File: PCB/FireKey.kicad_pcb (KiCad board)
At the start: 2 copper layers, 99.7 x 99.1 mm, 71 parts, among them P1 Pad, P2 Pad, SW1 SW_MEC_4A, U1 Arduino_Pro_Micro_USB-C

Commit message: finished rounting
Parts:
- moved P1 25.6 mm to (163.6, 48.8)
- moved P2 23.5 mm to (169.7, 48.8)
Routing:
- net VCC: track 516.5 -> 527.2 mm
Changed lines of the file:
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@@
   )
   (footprint "TestPoint:TestPoint_Pad_D2.5mm" (layer "B.Cu")
-    (at 169.418 25.273 180)
+    (at 169.672 48.768 180)
     (descr "SMD pad as test Point, diameter 2.5mm")
     (tags "test point SMD pad")
@@
   )
   (footprint "TestPoint:TestPoint_Pad_D2.5mm" (layer "B.Cu")
-    (at 173.99 25.4 180)
+    (at 163.576 48.768 180)
     (descr "SMD pad as test Point, diameter 2.5mm")
     (tags "test point SMD pad")
@@
     (effects (font (size 0.75 0.75) (thickness 0.16)) (justify mirror))
   )
-  (gr_text "VCC" (at 165.481 27.94) (layer "B.SilkS")
+  (gr_text "VCC" (at 163.576 51.308) (layer "B.SilkS")
     (effects (font (size 1 1) (thickness 0.2)) (justify mirror))
   )
@@
     (effects (font (size 0.75 0.75) (thickness 0.16)) (justify mirror))
   )
-  (gr_text "GND" (at 169.418 27.94) (layer "B.SilkS")
+  (gr_text "GND" (at 169.672 51.308) (layer "B.SilkS")
     (effects (font (size 1 1) (thickness 0.2)) (justify mirror))
   )
@@
   (segment (start 157.607 89.408) (end 156.8185 90.1965) (width 0.635) (layer "B.Cu") (net 1))
   (segment (start 179.445 129.425) (end 175.8805 129.425) (width 0.635) (layer "B.Cu") (net 1))
+  (segment (start 164.865 40.875) (end 163.576 42.164) (width 0.635) (layer "B.Cu") (net 1))
   (segment (start 203.995 40.875) (end 203.995 39.845) (width 0.635) (layer "B.Cu") (net 1))
   (segment (start 233.0305 91.325) (end 233.0185 91.313) (width 0.635) (layer "B.Cu") (net 1))
@@
   (segment (start 213.9685 90.1965) (end 214.757 89.408) (width 0.635) (layer "B.Cu") (net 1))
   (segment (start 176.657 127.508) (end 157.607 127.508) (width 0.635) (layer "B.Cu") (net 1))
+  (segment (start 163.576 42.164) (end 163.576 48.768) (width 0.635) (layer "B.Cu") (net 1))
   (segment (start 233.0185 129.413) (end 233.0185 128.2965) (width 0.635) (layer "B.Cu") (net 1))
   (segment (start 223.145 111.875) (end 226.7095 111.875) (width 0.635) (layer "B.Cu") (net 1))
@@
   (segment (start 217.545 91.325) (end 213.9805 91.325) (width 0.635) (layer "B.Cu") (net 1))
   (segment (start 175.8685 129.413) (end 175.8685 128.2965) (width 0.635) (layer "B.Cu") (net 1))
+  (segment (start 167.165 40.875) (end 164.865 40.875) (width 0.635) (layer "B.Cu") (net 1))
   (segment (start 203.995 39.845) (end 204.724 39.116) (width 0.635) (layer "B.Cu") (net 1))
   (segment (start 175.8805 91.325) (end 175.8685 91.313) (width 0.635) (layer "B.Cu") (net 1))

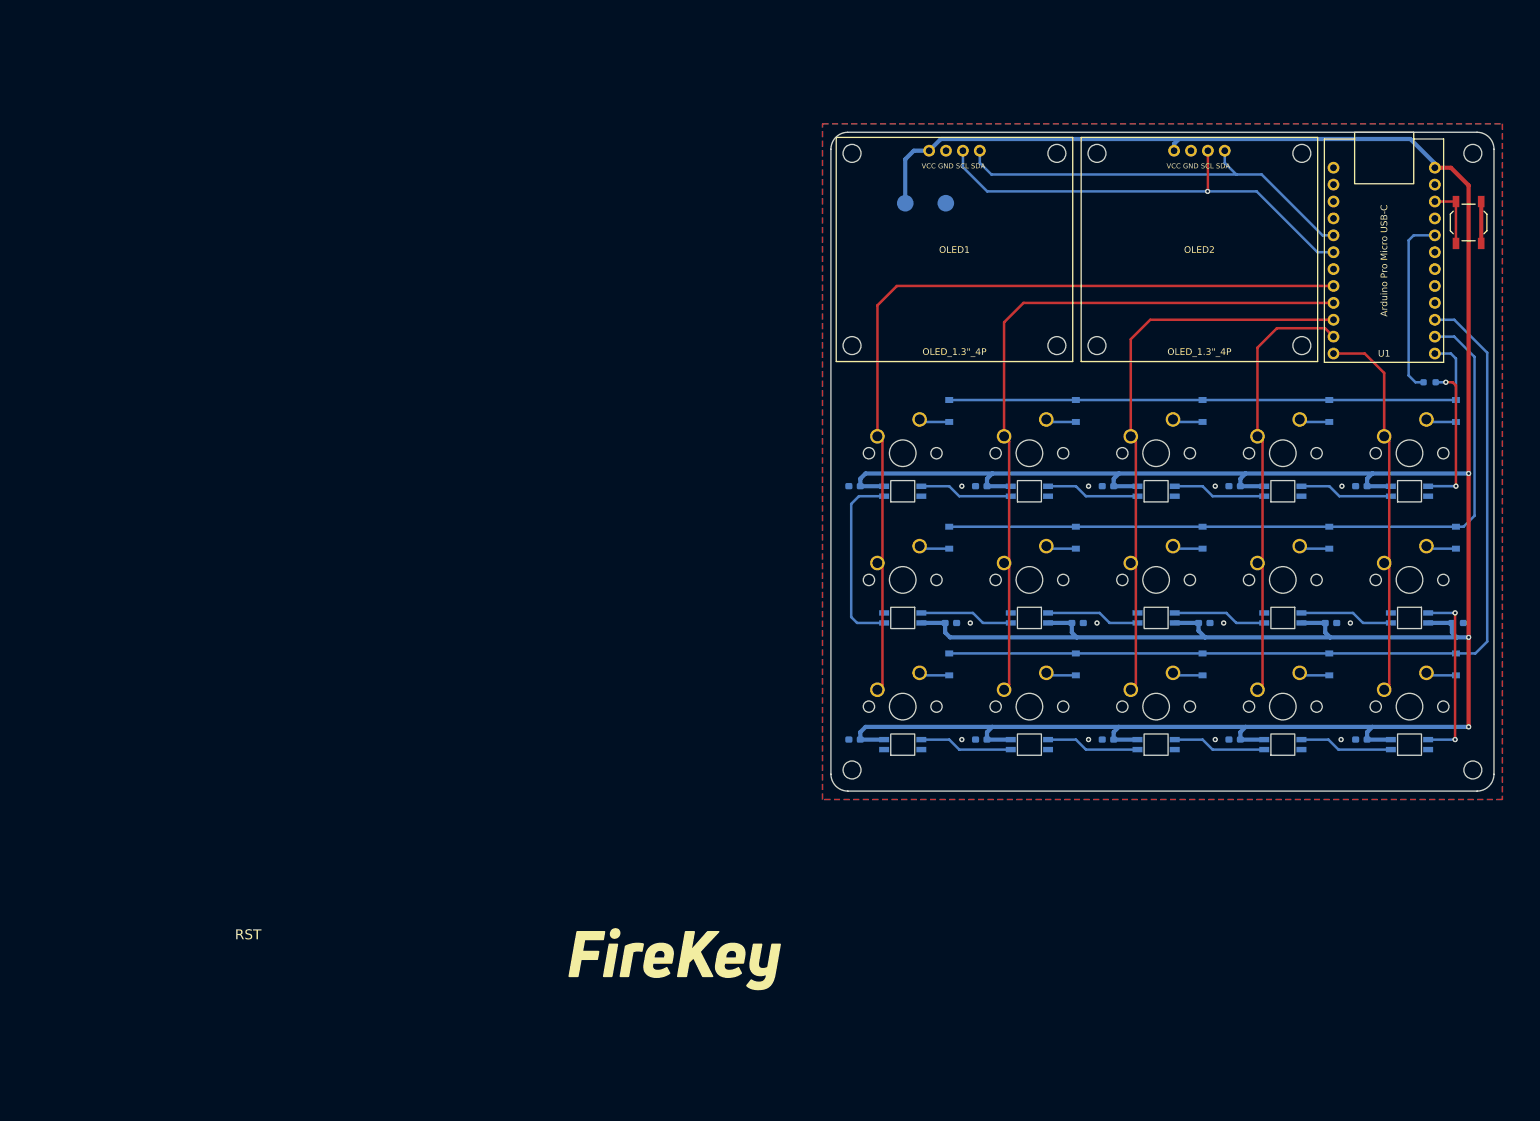
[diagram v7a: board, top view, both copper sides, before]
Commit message: small changes to PCB; placing logos
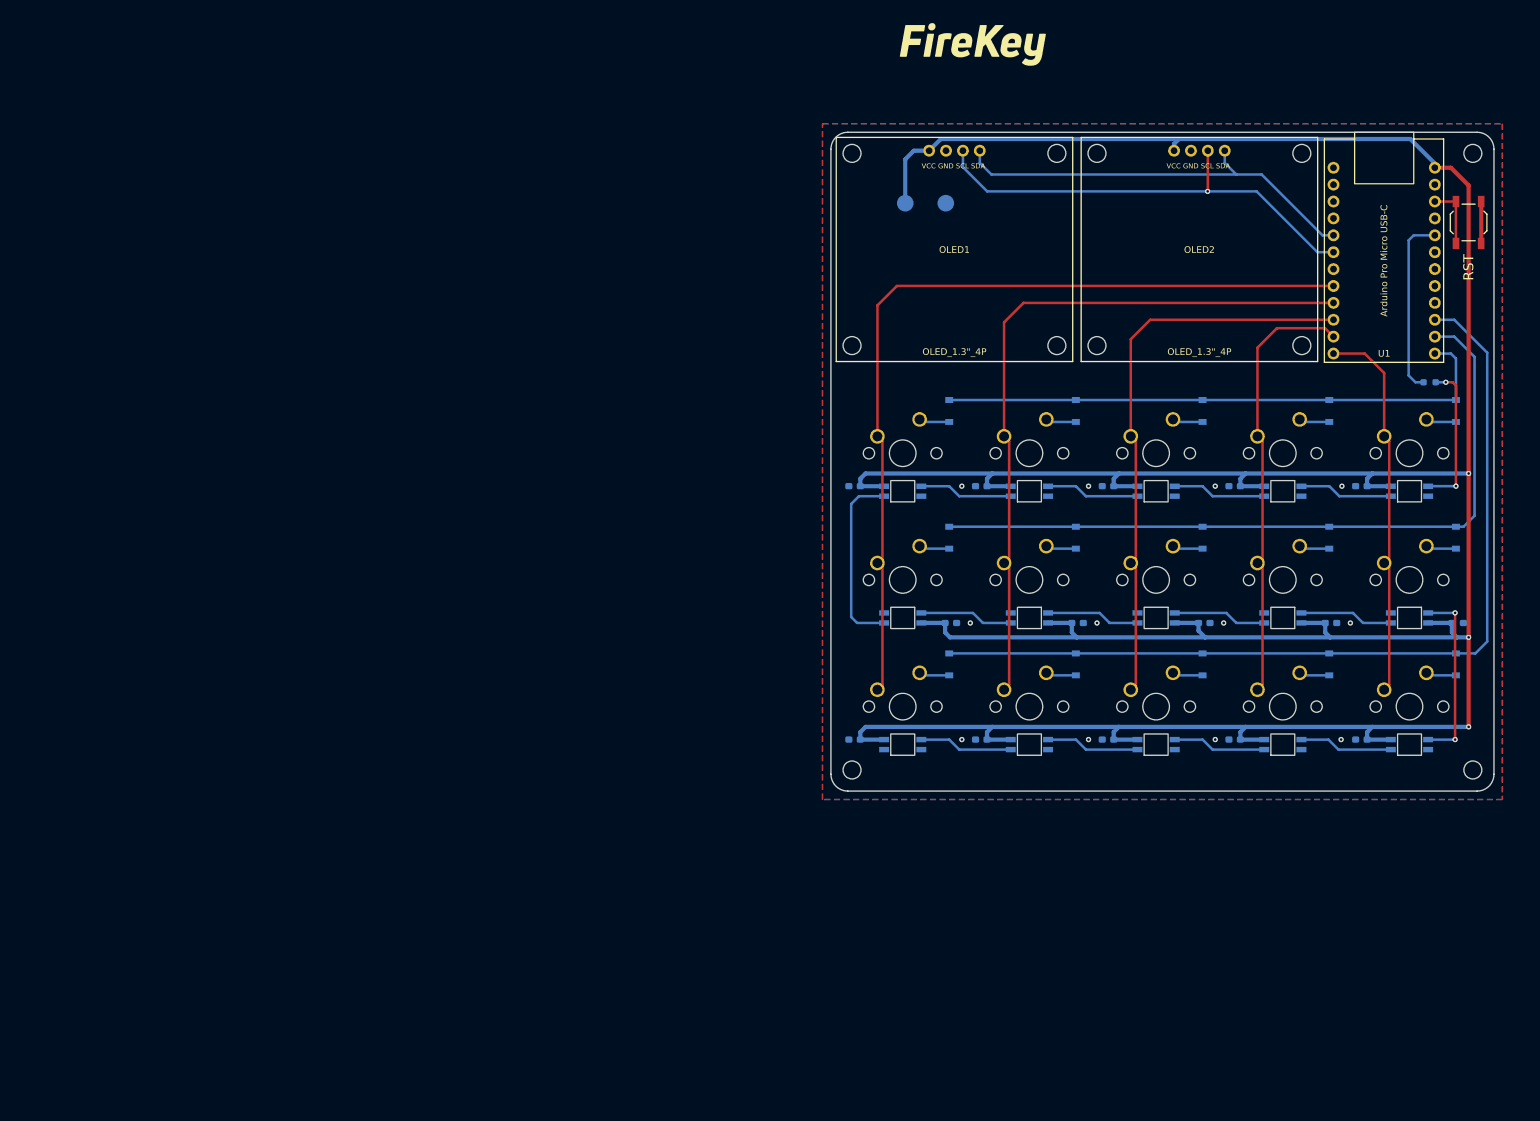
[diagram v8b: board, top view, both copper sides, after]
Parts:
- added Logo2: Logo_FireKey, Custom_FireKey:Logo_FireKey_22x6.4, F.Cu at (173.7, 24.9)
- Logo1: footprint Custom_FireKey:Logo_FireKey_32x9.4 -> Custom_FireKey:Logo_FireKey_22x6.4; moved to B.Cu
- moved Logo1 163.8 mm to (211.5, 21.0), turned to 180 degrees
